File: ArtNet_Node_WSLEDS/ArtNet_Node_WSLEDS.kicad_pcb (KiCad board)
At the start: 2 copper layers, 80.5 x 72.4 mm, 60 parts, among them J1 Conn_01x02_Female, J2 Conn_01x04_Female, J3 Conn_01x03_Male, J4 Conn_01x08_Male, J5 Conn_01x08_Male, Q1 BSS138, Q2 BSS138, Q3 BSS138, Q4 BSS138, Q5 BSS138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

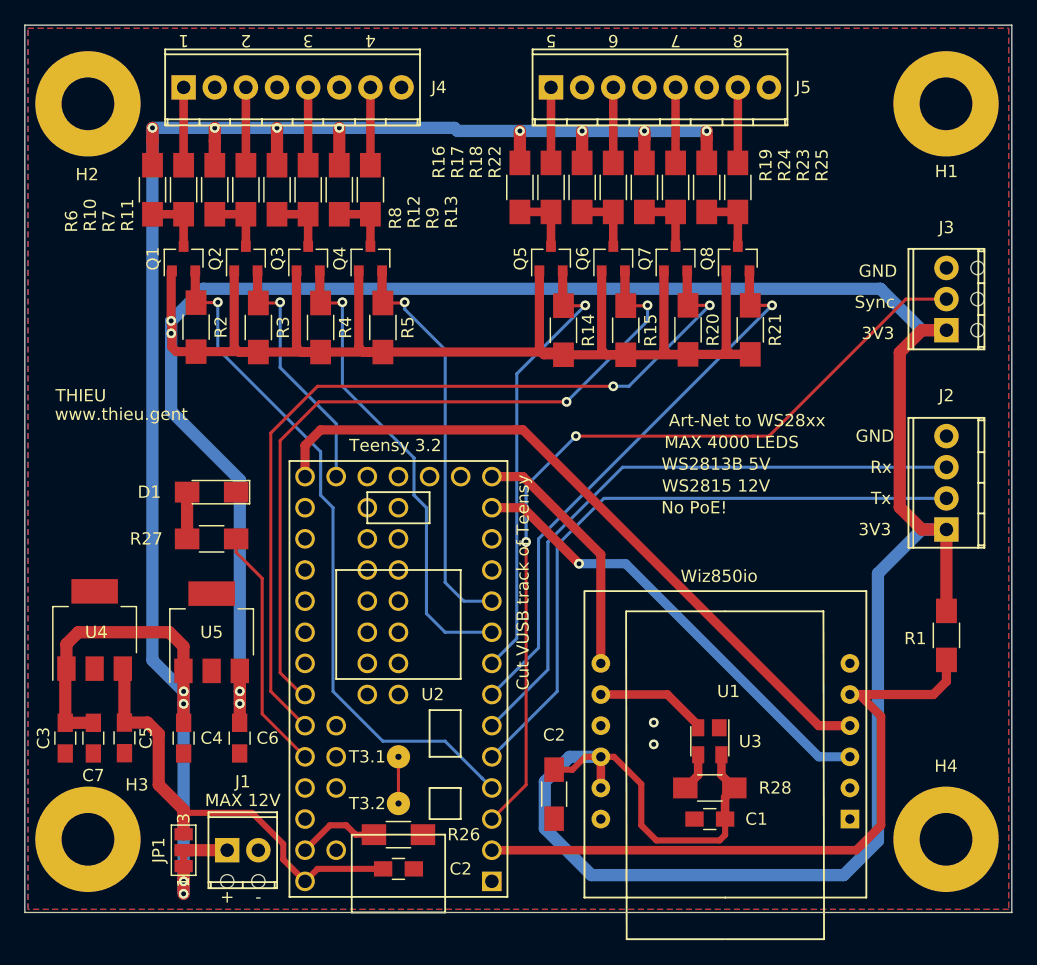
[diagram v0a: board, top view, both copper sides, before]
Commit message: Update the PCB design;
Migration to FastLED library (more reliable). And 4 more outputs which makes is 12 in total (+1 if soldered to R14).
Also change the output driver to 74HCT245. The mosfet solution was not working very on fast speeds.
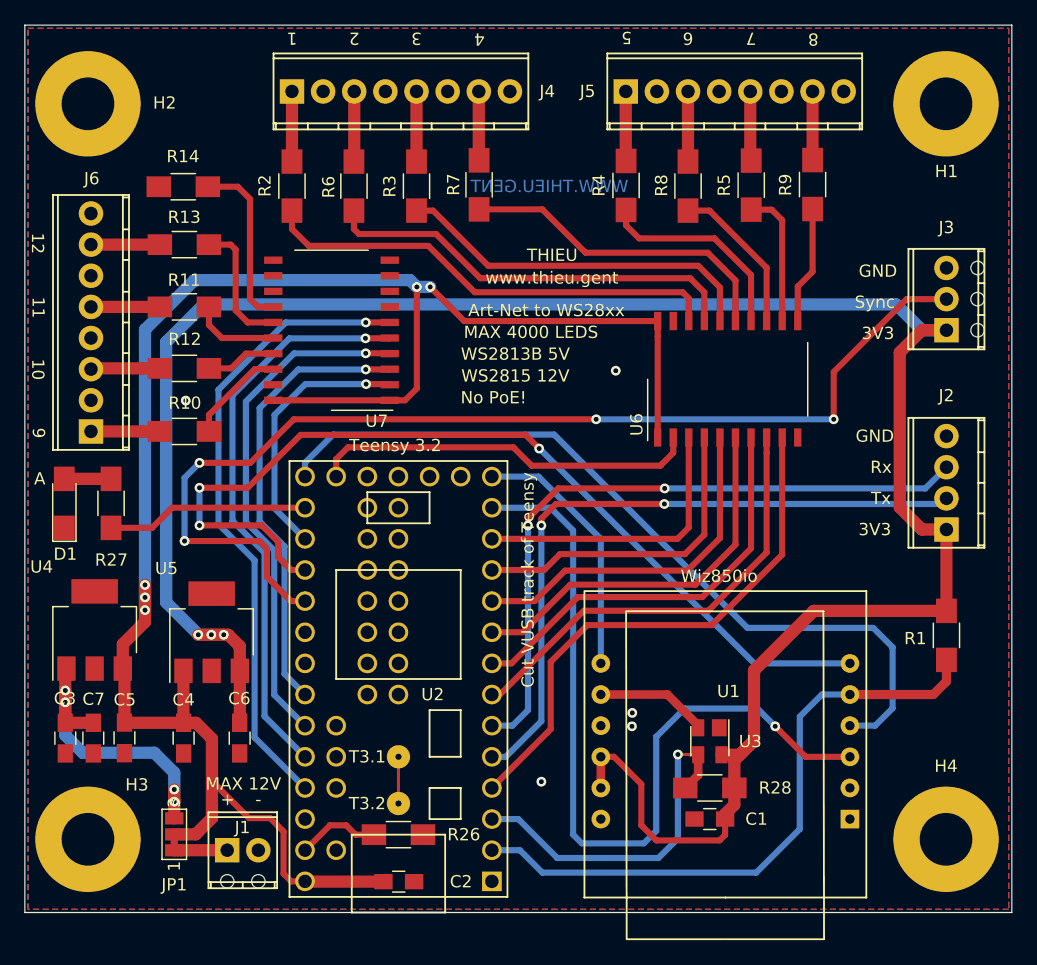
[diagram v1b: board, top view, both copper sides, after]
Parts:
- removed the C2 at (113.0, 131.3)
- removed Q1, Q2, Q3, Q4, Q5, Q6, Q7, Q8: BSS138, TO_SOT_Packages_SMD:SOT-23
- removed R15, R16, R17, R20, R21, R22, R23: 10k, Resistors_SMD:R_1206_HandSoldering
- removed R18, R19, R24, R25: 100R, Resistors_SMD:R_1206_HandSoldering
- added J6: Conn_01x08_Male, TerminalBlocks_Phoenix:TerminalBlock_Phoenix_MPT-2.54mm_8pol, F.Cu at (75.2, 101.7)
- added U6: 74HCT245, Housings_SOIC:SO-20_12.8x7.5mm_Pitch1.27mm, F.Cu at (127.2, 97.5)
- added U7: 74HCT245, Housings_SOIC:SO-20_12.8x7.5mm_Pitch1.27mm, F.Cu at (94.9, 93.5)
- R14, R2, R3, R4, R5, R6, R7, R8, R9: value 10k -> 100R
- R27: value 0R -> 120R
- U4, U5: footprint TO_SOT_Packages_SMD:SOT-223 -> TO_SOT_Packages_SMD:SOT-223-3_TabPin2
- moved R9 38.6 mm to (134.1, 81.6), turned to 270 degrees
- moved R8 33.5 mm to (124.0, 81.7), turned to 270 degrees
- moved R14 33.2 mm to (82.8, 81.8), turned to 0 degrees
- moved R5 32.2 mm to (129.1, 81.6)
- moved R4 27.5 mm to (118.9, 81.7)
- moved R7 21.6 mm to (106.9, 81.6), turned to 270 degrees
- moved R10 19.7 mm to (82.9, 101.7), turned to 0 degrees
- moved R12 17.7 mm to (82.9, 96.6), turned to 0 degrees
- moved R3 17.3 mm to (101.8, 81.7)
- moved R6 16.4 mm to (96.7, 81.7), turned to 270 degrees
- moved R13 15.8 mm to (82.9, 86.5), turned to 0 degrees
- moved R2 13.9 mm to (91.6, 81.7)
- moved D1 12.0 mm to (73.1, 107.6), turned to 90 degrees
- moved R11 10.8 mm to (82.9, 91.6), turned to 0 degrees
- moved J4 8.85 mm to (91.6, 74.0)
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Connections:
- C4 pad 1: +12V -> +5V
- JP1 pad 1: +12V -> Net-(J1-Pad1)
- JP1 pad 2: Net-(J1-Pad1) -> +5V
- JP1 pad 3: +5V -> +12V
- R10 pad 1: LED1_OUT -> LED9_OUT
- R10 pad 2: Net-(Q1-Pad3) -> Net-(R10-Pad2)
- R11 pad 1: LED2_OUT -> LED11_OUT
- R11 pad 2: Net-(Q2-Pad3) -> Net-(R11-Pad2)
- R12 pad 1: LED3_OUT -> LED10_OUT
- R12 pad 2: Net-(Q3-Pad3) -> Net-(R12-Pad2)
- R13 pad 1: LED4_OUT -> LED12_OUT
- R13 pad 2: Net-(Q4-Pad3) -> Net-(R13-Pad2)
- R14 pad 1: LED5 -> Net-(R14-Pad1)
- R14 pad 2: +3V3 -> Net-(R14-Pad2)
- R2 pad 1: LED1 -> LED1_OUT
- R2 pad 2: +3V3 -> Net-(R2-Pad2)
- R28 pad 1: Net-(R28-Pad1) -> WIZ_RESET
- R3 pad 1: LED2 -> LED3_OUT
- R3 pad 2: +3V3 -> Net-(R3-Pad2)
- R4 pad 1: LED3 -> LED5_OUT
- R4 pad 2: +3V3 -> Net-(R4-Pad2)
- R5 pad 1: LED4 -> LED7_OUT
- R5 pad 2: +3V3 -> Net-(R5-Pad2)
- R6 pad 1: Net-(Q1-Pad3) -> LED2_OUT
- R6 pad 2: +12V -> Net-(R6-Pad2)
- R7 pad 1: Net-(Q2-Pad3) -> LED4_OUT
- R7 pad 2: +12V -> Net-(R7-Pad2)
- R8 pad 1: Net-(Q3-Pad3) -> LED6_OUT
- R8 pad 2: +12V -> Net-(R8-Pad2)
- R9 pad 1: Net-(Q4-Pad3) -> LED8_OUT
- R9 pad 2: +12V -> Net-(R9-Pad2)
- U1 pad 6: Net-(U1-Pad6) -> INT
- U2 pad 11: Net-(U2-Pad11) -> LED3
- U2 pad 12: Net-(U2-Pad12) -> LED2
- U2 pad 17: Net-(U2-Pad17) -> GND
- U2 pad 19: LED2 -> LED1
- U2 pad 21: Net-(U2-Pad21) -> HAPPY
- U2 pad 22: Net-(U2-Pad22) -> LED9
- U2 pad 23: Net-(U2-Pad23) -> INT
- U2 pad 24: Net-(U2-Pad24) -> FrameSync
- U2 pad 27: LED6 -> LED10
- U2 pad 28: LED7 -> LED11
- U2 pad 29: HAPPY -> LED12
- U2 pad 3: FrameSync -> WIZ_RESET
- U2 pad 30: Net-(U2-Pad30) -> LED13
- U2 pad 4: LED1 -> LED8
- U2 pad 7: LED8 -> LED7
- U2 pad 8: LED5 -> LED6
- U2 pad 9: LED3 -> LED5
- U3 pad 3: Net-(R28-Pad1) -> WIZ_RESET
- U5 pad 1: +12V -> +5V
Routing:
- net +3V3: track 342.2 -> 184.1 mm, vias 4 -> 3
- net +12V: track 159.1 -> 25.3 mm, vias 12 -> 4
- net +5V: track 36.8 -> 151.1 mm, vias 0 -> 5
- net INT: track 0.00 -> 76.5 mm, vias 0 -> 3
- net LED13: track 0.00 -> 51.7 mm, vias 0 -> 1
- net LED12: track 0.00 -> 46.7 mm, vias 0 -> 1
- net LED11: track 0.00 -> 41.8 mm, vias 0 -> 1
- net Net-(R2-Pad2): track 0.00 -> 38.1 mm
- net LED10: track 0.00 -> 36.8 mm, vias 0 -> 1
- net Net-(R6-Pad2): track 0.00 -> 34.6 mm
- net LED7: track 69.8 -> 36.6 mm, vias 2 -> 0
- net Net-(R3-Pad2): track 0.00 -> 30.1 mm
- net WIZ_RESET: track 0.00 -> 28.8 mm, vias 0 -> 1
- net MOSI: track 37.6 -> 65.8 mm
- net LED6: track 61.4 -> 34.1 mm, vias 2 -> 0
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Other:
- board text added: "10"
- board text added: "11"
- board text added: "12"
- board text added: "9"
- board text added: "A"
- board text added: "WWW.THIEU.GENT"
